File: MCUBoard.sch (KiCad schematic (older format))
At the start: 61 parts, among them J1 USB_B_Micro, J2 Conn_01x04, J3 Conn_02x03_Odd_Even, J4 Conn_02x05_Odd_Even, J5 Conn_01x04, J6 Conn_01x04, J7 Conn_01x16, J8 Conn_02x16_Odd_Even, J9 Conn_01x04, Q1 BSS138, Q2 BSS138, Q3 BSS138, Q4 BSS138, SW1 SW_Push, U1 LM324A, U3 STM32F103C8Tx, U4 LT1962-3.3, Y1 8MHz, Y2 32.768KHz

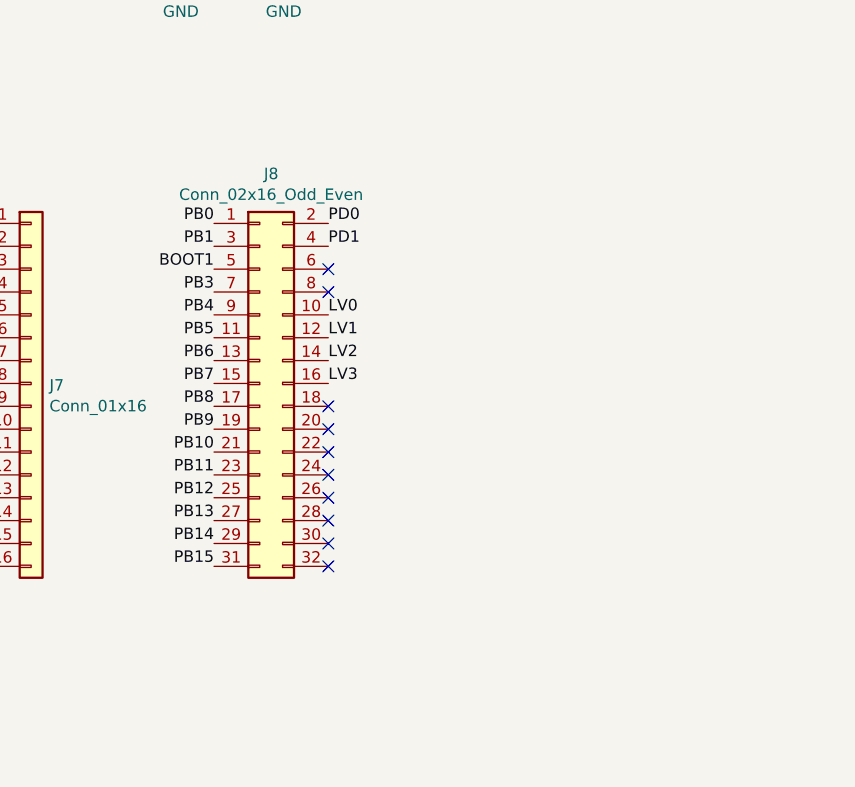
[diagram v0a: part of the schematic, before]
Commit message: change PB headers and route tracks for port B
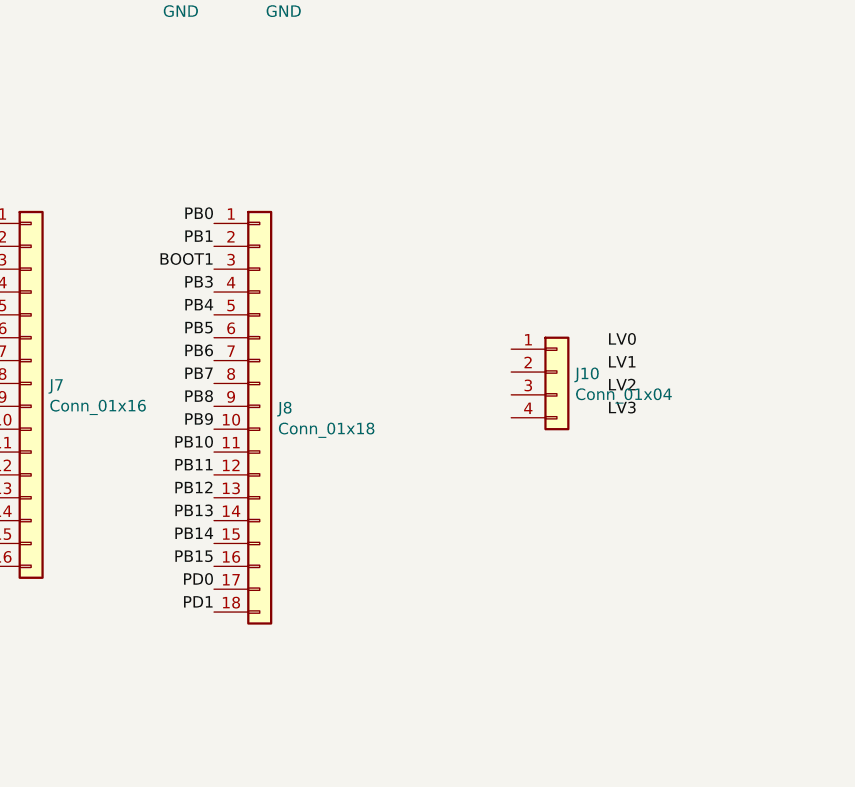
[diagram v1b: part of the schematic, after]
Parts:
- removed J8: Conn_02x16_Odd_Even, Connector_PinHeader_2.54mm:PinHeader_2x16_P2.54mm_Vertical, symbol Connector_Generic:Conn_02x16_Odd_Even
- added J10: Conn_01x04, Connector_PinHeader_2.54mm:PinHeader_1x04_P2.54mm_Vertical, symbol Connector_Generic:Conn_01x04
- added J8: Conn_01x18, Connector_PinHeader_2.54mm:PinHeader_1x18_P2.54mm_Vertical, symbol Connector_Generic:Conn_01x18
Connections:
- net BOOT1: now also J8.3 (Pin_3)
- net PB0: now also J8.1 (Pin_1)
- net PB1: now also J8.2 (Pin_2)
- net PB10: now also J8.11 (Pin_11)
- net PB11: now also J8.12 (Pin_12)
- net PB12: now also J8.13 (Pin_13)
- net PB13: now also J8.14 (Pin_14)
- net PB14: now also J8.15 (Pin_15)
- net PB15: now also J8.16 (Pin_16)
- net PB3: now also J8.4 (Pin_4)
- net PB4: now also J8.5 (Pin_5)
- net PB5: now also J8.6 (Pin_6)
- net PB6: now also J8.7 (Pin_7)
- net PB7: now also J8.8 (Pin_8)
- net PB8: now also J8.9 (Pin_9)
- net PB9: now also J8.10 (Pin_10)
- net PD0: now also J8.17 (Pin_17)
- net PD1: now also J8.18 (Pin_18)
- no-connect marks 16 -> 6
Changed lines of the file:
@@
 Text Label 11200 4600 0    50   ~ 0
 LV3
-Text Label 6300 7500 0    50   ~ 0
+Text Label 7650 7650 2    50   ~ 0
 LV0
-Text Label 6300 7600 0    50   ~ 0
+Text Label 7650 7750 2    50   ~ 0
 LV1
-Text Label 6300 7700 0    50   ~ 0
+Text Label 7650 7850 2    50   ~ 0
 LV2
-Text Label 6300 7800 0    50   ~ 0
+Text Label 7650 7950 2    50   ~ 0
 LV3
 $Comp
@@
 Text Label 3550 1600 0    50   ~ 0
 NRST
-Text Label 6300 7100 0    50   ~ 0
+Text Label 5800 8700 2    50   ~ 0
 PD0
-Text Label 6300 7200 0    50   ~ 0
+Text Label 5800 8800 2    50   ~ 0
 PD1
-NoConn ~ 6300 7300
-NoConn ~ 6300 7400
-NoConn ~ 6300 7900
-NoConn ~ 6300 8000
-NoConn ~ 6300 8100
-NoConn ~ 6300 8200
-NoConn ~ 6300 8300
-NoConn ~ 6300 8400
-NoConn ~ 6300 8500
-NoConn ~ 6300 8600
 NoConn ~ 3750 900
 $Comp
@@
 Connection ~ 4100 1200
 $Comp
-L Connector_Generic:Conn_02x16_Odd_Even J8
-U 1 1 5C857FFA
-P 6000 7800
-F 0 "J8" H 6050 8717 50  0000 C CNN
-F 1 "Conn_02x16_Odd_Even" H 6050 8626 50  0000 C CNN
-F 2 "Connector_PinHeader_2.54mm:PinHeader_2x16_P2.54mm_Vertical" H 6000 7800 50  0001 C CNN
-F 3 "~" H 6000 7800 50  0001 C CNN
-	1    6000 7800
+L Connector_Generic:Conn_01x18 J8
+U 1 1 5C85ACFE
+P 6000 7900
+F 0 "J8" H 6080 7892 50  0000 L CNN
+F 1 "Conn_01x18" H 6080 7801 50  0000 L CNN
+F 2 "Connector_PinHeader_2.54mm:PinHeader_1x18_P2.54mm_Vertical" H 6000 7900 50  0001 C CNN
+F 3 "~" H 6000 7900 50  0001 C CNN
+	1    6000 7900
 	1    0    0    -1
 $EndComp
+$Comp
+L Connector_Generic:Conn_01x04 J10
+U 1 1 5C85AF00
+P 7300 7750
+F 0 "J10" H 7380 7742 50  0000 L CNN
+F 1 "Conn_01x04" H 7380 7651 50  0000 L CNN
+F 2 "Connector_PinHeader_2.54mm:PinHeader_1x04_P2.54mm_Vertical" H 7300 7750 50  0001 C CNN
+F 3 "~" H 7300 7750 50  0001 C CNN
+	1    7300 7750
+	1    0    0    -1
+$EndComp

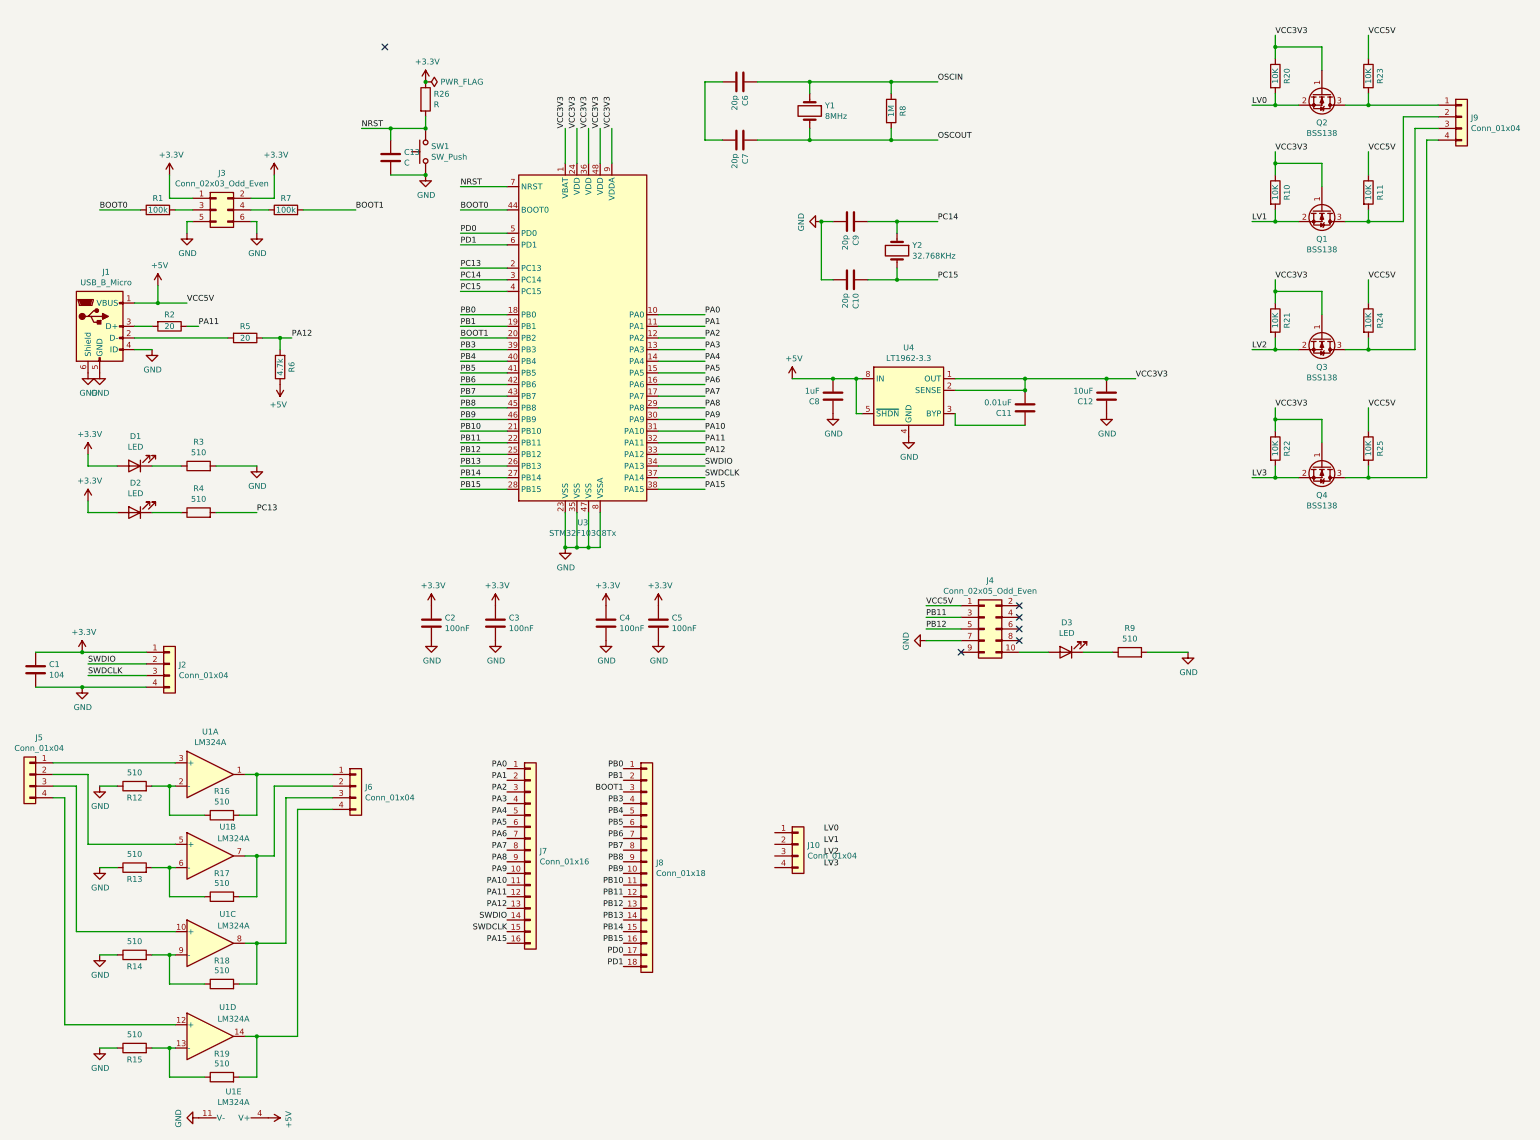
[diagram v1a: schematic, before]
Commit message: route all non-power tracks
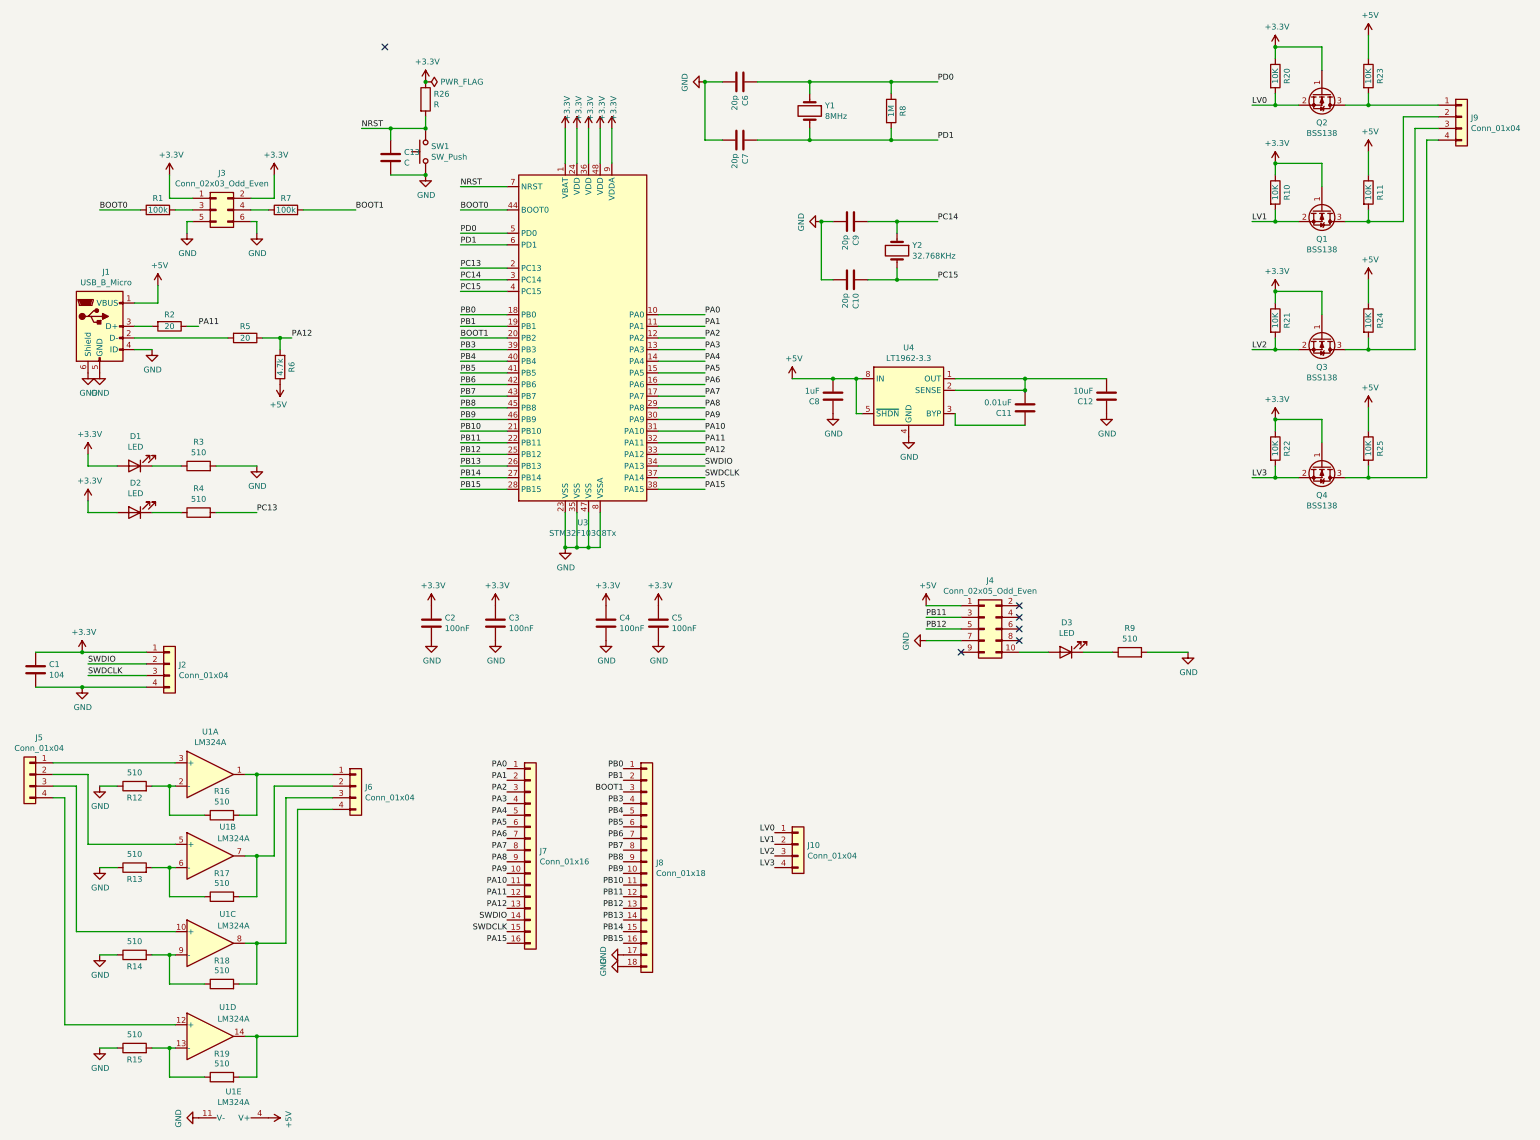
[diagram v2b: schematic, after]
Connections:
- net OSCIN is gone; now on net PD0: C6.1, R8.1, Y1.1
- net OSCOUT is gone; now on net PD1: C7.1, R8.2, Y1.2
- net +3V3: now also Q1.1 (G), Q2.1 (G), Q3.1 (G), Q4.1 (G), R10.1, R20.1, R21.1, R22.1, U3.1 (VBAT), U3.24 (VDD), U3.36 (VDD), U3.48 (VDD), U3.9 (VDDA)
- net GND: now also C6.2, C7.2, J8.17 (Pin_17), J8.18 (Pin_18)
- net LV0: now also J10.1 (Pin_1)
- net LV1: now also J10.2 (Pin_2)
- net LV2: now also J10.3 (Pin_3)
- net LV3: now also J10.4 (Pin_4)
- net PD0: no longer J8.17 (Pin_17)
- net PD1: no longer J8.18 (Pin_18)
- removed net VCC3V3: C11.2, C12.2, Q1.1 (G), Q2.1 (G), Q3.1 (G), Q4.1 (G), R10.1, R20.1, R21.1, R22.1, U3.1 (VBAT), U3.24 (VDD), U3.36 (VDD), U3.48 (VDD), U3.9 (VDDA), U4.1 (OUT), U4.2 (SENSE)
- new net: C11.2, C12.2, U4.1 (OUT), U4.2 (SENSE)

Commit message: board routed
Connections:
- net +3V3: now also C11.2, C12.2, U4.1 (OUT), U4.2 (SENSE)
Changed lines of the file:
@@
+	1    0    0    -1
+$EndComp
+$Comp
+L power:+3.3V #PWR?
+U 1 1 5C874990
+P 9250 3750
+F 0 "#PWR?" H 9250 3600 50  0001 C CNN
+F 1 "+3.3V" H 9265 3923 50  0000 C CNN
+F 2 "" H 9250 3750 50  0001 C CNN
+F 3 "" H 9250 3750 50  0001 C CNN
+	1    9250 3750
 	1    0    0    -1
 $EndComp
